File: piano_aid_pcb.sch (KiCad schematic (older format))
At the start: 25 parts, among them J1 Barrel_Jack_MountingPin, J2 Screw_Terminal_01x03, J3 DIN-5_180degree, J4 Conn_01x06_Female, J5 Micro_SD_Card, U1 317030213, U2 6N138, U3 74AHCT1G125SE-7, U4 AZ1117-3.3

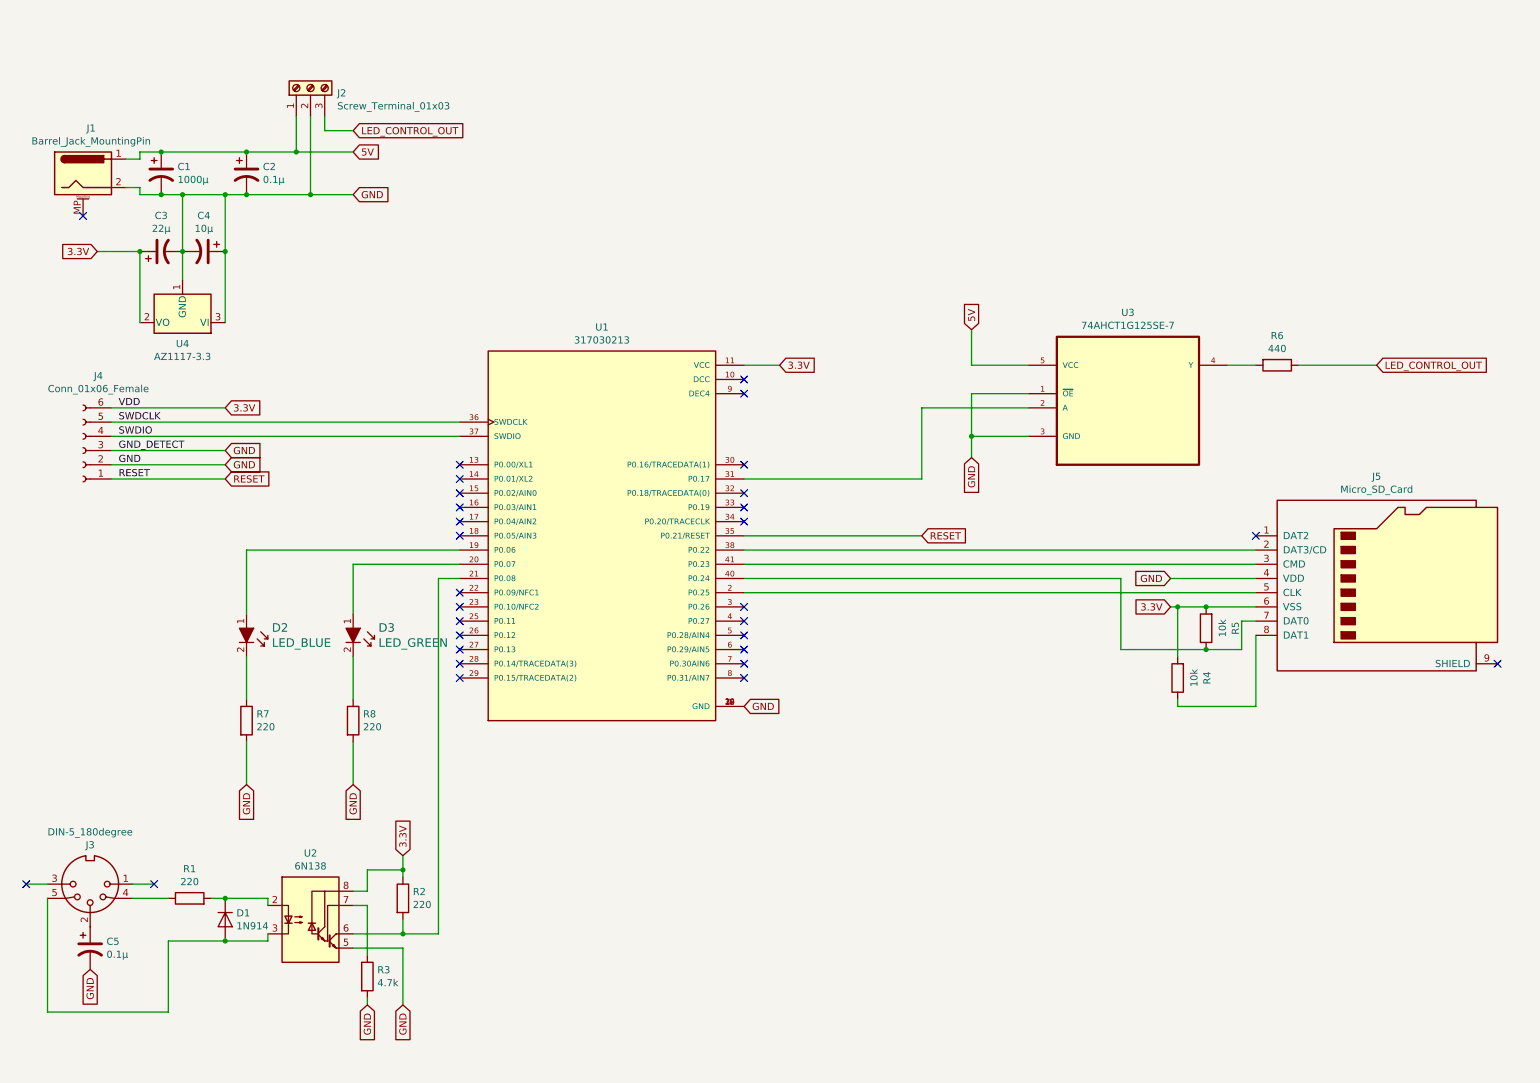
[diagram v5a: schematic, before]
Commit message: Started board layout. Finished footprints
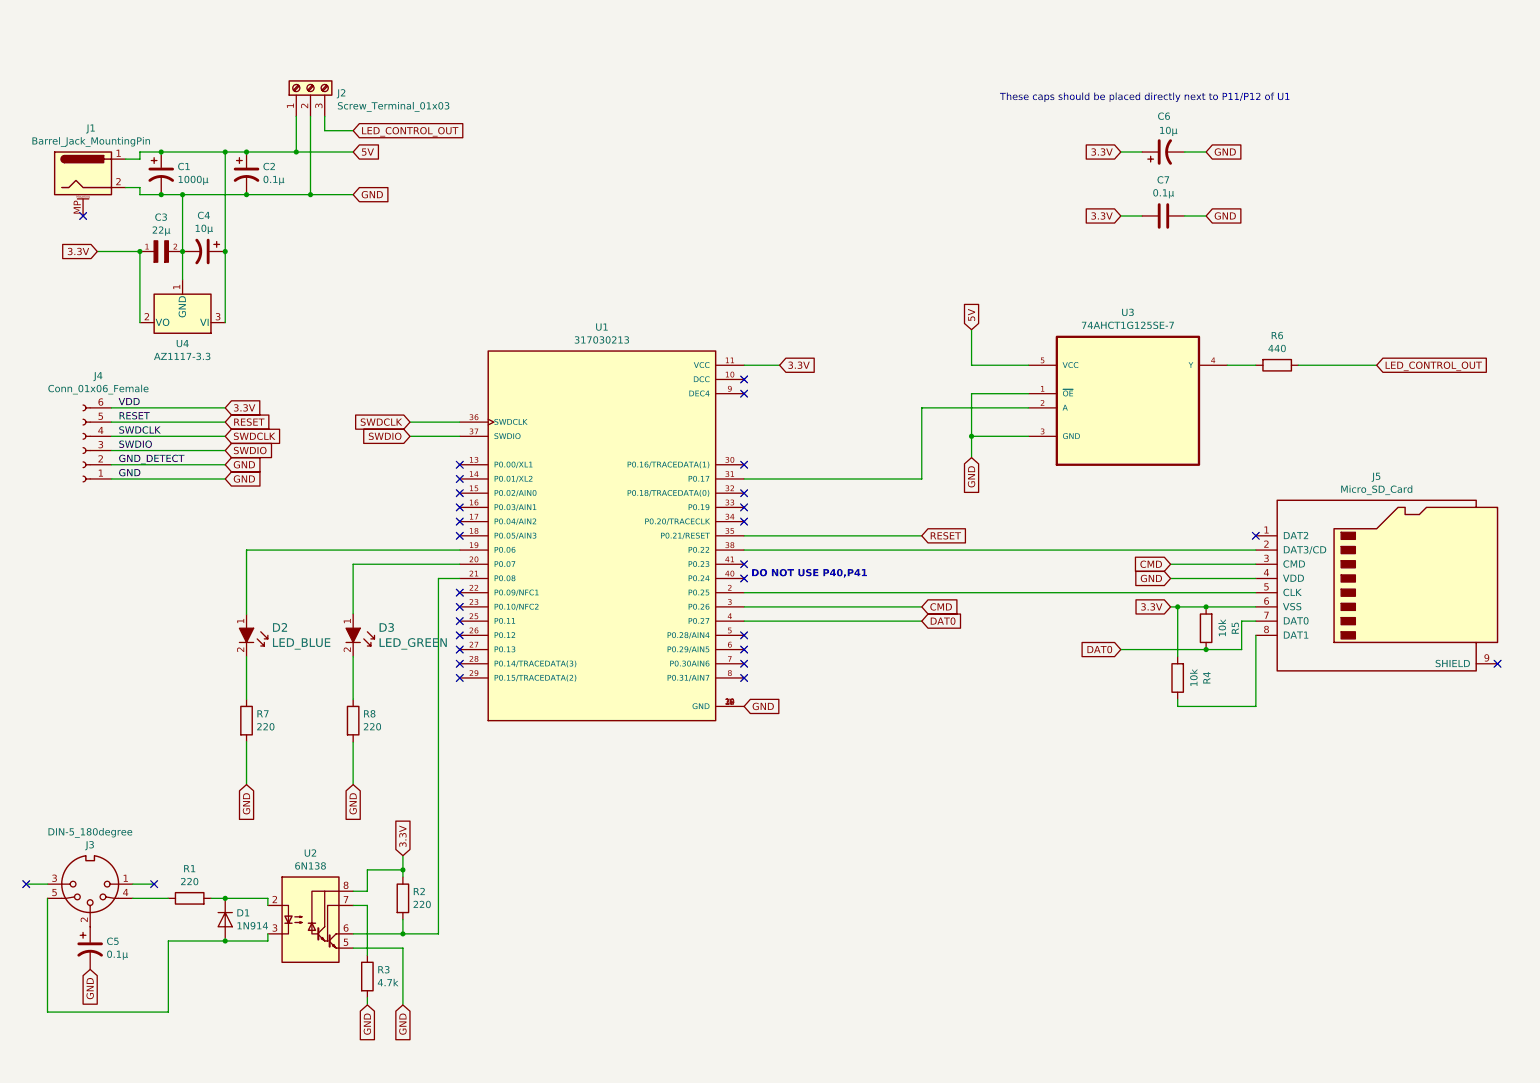
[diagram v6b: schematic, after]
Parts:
- removed C3: 22µ, symbol Device:CP1
- added C3: 22µ, C1206C226M9PACTU:CAPC3216X110N, symbol C1206C226M9PACTU:C1206C226M9PACTU
- added C6: 10µ, Capacitor_SMD:C_0805_2012Metric_Pad1.15x1.40mm_HandSolder, symbol Device:CP1
- added C7: 0.1µ, Capacitor_SMD:C_0805_2012Metric_Pad1.15x1.40mm_HandSolder, symbol Device:C
- C1: footprint (none) -> Capacitor_THT:CP_Radial_D10.0mm_P5.00mm
- C2, C4, C5: footprint (none) -> Capacitor_SMD:C_0805_2012Metric_Pad1.15x1.40mm_HandSolder
- D2, D3: footprint digikey-footprints:0603 -> LED_SMD:LED_0805_2012Metric_Pad1.15x1.40mm_HandSolder
- J4: footprint (none) -> Connector_PinSocket_2.54mm:PinSocket_1x06_P2.54mm_Vertical
- U2: footprint (none) -> Package_DIP:DIP-8_W7.62mm
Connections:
- net 3.3V: now also C3.1, C6.1, C7.2
- net 5V: now also C4.1, U4.3 (VI)
- net GND: now also J4.1 (Pin_1), C3.2, C6.2, C7.1; no longer C4.1, J4.3 (Pin_3), U4.3 (VI)
- net RESET: now also J4.5 (Pin_5); no longer J4.1 (Pin_1)
- net SWDCLK: now also J4.4 (Pin_4); no longer J4.5 (Pin_5)
- net SWDIO: now also J4.3 (Pin_3); no longer J4.4 (Pin_4)
- net CMD: now reaches U1.3 (P0.26)
- net CMD: now also J5.3 (CMD)
- net DAT0: now reaches U1.4 (P0.27)
- net DAT0: now also J5.7 (DAT0), R5.1
- net at U1.41 (P0.23): no longer J5.3 (CMD)
- now unconnected: U1.40 (P0.24)
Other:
- note added: "DO NOT USE P40,P41"
- note added: "These caps should be placed directly next to P11/P12 of U1"
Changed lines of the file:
@@
 F 0 "C1" H 1665 1196 50  0000 L CNN
 F 1 "1000µ" H 1665 1105 50  0000 L CNN
-F 2 "" H 1550 1150 50  0001 C CNN
+F 2 "Capacitor_THT:CP_Radial_D10.0mm_P5.00mm" H 1550 1150 50  0001 C CNN
 F 3 "~" H 1550 1150 50  0001 C CNN
 	1    1550 1150
@@
 	1400 1300 1550 1300
 Wire Wire Line
-	1200 2900 3650 2900
-Wire Wire Line
-	3650 3000 1200 3000
-Wire Wire Line
 	5650 3700 6900 3700
 $Comp
@@
 F 0 "J4" H 892 2575 50  0000 C CNN
 F 1 "Conn_01x06_Female" H 892 2666 50  0000 C CNN
-F 2 "" H 1000 3100 50  0001 C CNN
+F 2 "Connector_PinSocket_2.54mm:PinSocket_1x06_P2.54mm_Vertical" H 1000 3100 50  0001 C CNN
 F 3 "~" H 1000 3100 50  0001 C CNN
 	1    1000 3100
@@
 Text Label 1250 2800 0    50   ~ 0
 VDD
+Text Label 1250 3000 0    50   ~ 0
+SWDCLK
+Text Label 1250 3100 0    50   ~ 0
+SWDIO
+Wire Wire Line
+	1200 3300 2000 3300
+Text Label 1250 3300 0    50   ~ 0
+GND
+Text Label 1250 3200 0    50   ~ 0
+GND_DETECT
 Text Label 1250 2900 0    50   ~ 0
-SWDCLK
-Text Label 1250 3000 0    50   ~ 0
-SWDIO
-Wire Wire Line
-	1200 3200 2000 3200
-Text Label 1250 3200 0    50   ~ 0
-GND
-Text Label 1250 3100 0    50   ~ 0
-GND_DETECT
-Text Label 1250 3300 0    50   ~ 0
 RESET
 $Comp
@@
 $EndComp
 Wire Wire Line
-	1200 3100 2000 3100
+	1200 3200 2000 3200
 Text GLabel 2900 1000 2    50   Input ~ 0
 5V
@@
 Text GLabel 5650 4900 2    50   Input ~ 0
 GND
-Text GLabel 2000 3100 2    50   Input ~ 0
-GND
 Text GLabel 2000 3200 2    50   Input ~ 0
+GND
+Text GLabel 2000 3300 2    50   Input ~ 0
 GND
 Text GLabel 8650 4000 0    50   Input ~ 0
@@
 NoConn ~ 9250 3700
 Wire Wire Line
-	9250 3900 5650 3900
-Wire Wire Line
 	9250 4100 5650 4100
 Wire Wire Line
@@
 	9150 4300 9150 4500
 Connection ~ 8900 4500
-Wire Wire Line
-	8300 4000 8300 4500
-Wire Wire Line
-	5650 4000 8300 4000
 Wire Wire Line
 	8300 4500 8900 4500
@@
 	1550 1300 1700 1300
 Connection ~ 1700 1300
-Wire Wire Line
-	1700 1300 2000 1300
-Connection ~ 2000 1300
 $Comp
 L Device:CP1 C4
@@
 F 0 "C4" V 1598 1700 50  0000 C CNN
 F 1 "10µ" V 1689 1700 50  0000 C CNN
-F 2 "" H 1850 1700 50  0001 C CNN
+F 2 "Capacitor_SMD:C_0805_2012Metric_Pad1.15x1.40mm_HandSolder" H 1850 1700 50  0001 C CNN
 F 3 "~" H 1850 1700 50  0001 C CNN
 	1    1850 1700
 	0    1    1    0
 $EndComp
-$Comp
-L Device:CP1 C3
-U 1 1 6145E06D
-P 1550 1700
-F 0 "C3" V 1802 1700 50  0000 C CNN
-F 1 "22µ" V 1711 1700 50  0000 C CNN
-F 2 "" H 1550 1700 50  0001 C CNN
-F 3 "~" H 1550 1700 50  0001 C CNN
-	1    1550 1700
-	0    -1   -1   0
-$EndComp
 Connection ~ 2000 1700
 Wire Wire Line
@@
 Wire Wire Line
 	1400 1700 1400 2200
-Wire Wire Line
-	2000 1300 2000 1700
 Wire Wire Line
 	1700 1300 1700 1700
@@
 3.3V
 Wire Wire Line
-	1550 1000 2150 1000
+	1550 1000 2000 1000
 Wire Wire Line
 	2500 1000 2900 1000
@@
 Wire Wire Line
 	2600 1300 2900 1300
-Wire Wire Line
-	2000 1300 2150 1300
 Connection ~ 2600 1300
 Wire Wire Line
@@
 Text GLabel 6900 3700 2    50   Input ~ 0
 RESET
-Text GLabel 2000 3300 2    50   Input ~ 0
+Text GLabel 2000 2900 2    50   Input ~ 0
 RESET
 Wire Wire Line
-	1200 3300 2000 3300
+	1200 2900 2000 2900
 $Comp
 L Device:CP1 C2
@@
 F 0 "C2" H 2265 1196 50  0000 L CNN
 F 1 "0.1µ" H 2265 1105 50  0000 L CNN
-F 2 "" H 2150 1150 50  0001 C CNN
+F 2 "Capacitor_SMD:C_0805_2012Metric_Pad1.15x1.40mm_HandSolder" H 2150 1150 50  0001 C CNN
 F 3 "~" H 2150 1150 50  0001 C CNN
 	1    2150 1150
@@
 F 0 "C5" H 1165 6646 50  0000 L CNN
 F 1 "0.1µ" H 1165 6555 50  0000 L CNN
-F 2 "" H 1050 6600 50  0001 C CNN
+F 2 "Capacitor_SMD:C_0805_2012Metric_Pad1.15x1.40mm_HandSolder" H 1050 6600 50  0001 C CNN
 F 3 "~" H 1050 6600 50  0001 C CNN
 	1    1050 6600
@@
 F 0 "U2" H 2600 6867 50  0000 C CNN
 F 1 "6N138" H 2600 6776 50  0000 C CNN
-F 2 "" H 2890 6100 50  0001 C CNN
+F 2 "Package_DIP:DIP-8_W7.62mm" H 2890 6100 50  0001 C CNN
 F 3 "http://www.onsemi.com/pub/Collateral/HCPL2731-D.pdf" H 2890 6100 50  0001 C CNN
 	1    2600 6400
@@
 NoConn ~ 5650 3500
 NoConn ~ 5650 3600
-NoConn ~ 5650 4200
-NoConn ~ 5650 4300
 NoConn ~ 5650 4400
 NoConn ~ 5650 4500
@@
 F 0 "D2" V 2047 4628 60  0000 L CNN
 F 1 "LED_BLUE" V 2153 4628 60  0000 L CNN
-F 2 "digikey-footprints:0603" H 2350 4650 60  0001 L CNN
+F 2 "LED_SMD:LED_0805_2012Metric_Pad1.15x1.40mm_HandSolder" H 2350 4650 60  0001 L CNN
 F 3 "http://optoelectronics.liteon.com/upload/download/DS22-2000-230/LTST-C191TBKT.pdf" H 2350 4750 60  0001 L CNN
 F 4 "160-1647-1-ND" H 2350 4850 60  0001 L CNN "Digi-Key_PN"
@@
 F 0 "D3" V 2797 4628 60  0000 L CNN
 F 1 "LED_GREEN" V 2903 4628 60  0000 L CNN
-F 2 "digikey-footprints:0603" H 3100 4650 60  0001 L CNN
+F 2 "LED_SMD:LED_0805_2012Metric_Pad1.15x1.40mm_HandSolder" H 3100 4650 60  0001 L CNN
 F 3 "https://dammedia.osram.info/media/resource/hires/osram-dam-2493945/LG%20L29K.pdf" H 3100 4750 60  0001 L CNN
 F 4 "475-2709-1-ND" H 3100 4850 60  0001 L CNN "Digi-Key_PN"
@@
 	0    1    1    0
 $EndComp
+Text GLabel 8300 1000 0    50   Input ~ 0
+3.3V
+Text GLabel 8900 1000 2    50   Input ~ 0
+GND
+$Comp
+L Device:CP1 C6
+U 1 1 614E35CA
+P 8600 1000
+F 0 "C6" V 8850 950 50  0000 L CNN
+F 1 "10µ" V 8750 900 50  0000 L CNN
+F 2 "Capacitor_SMD:C_0805_2012Metric_Pad1.15x1.40mm_HandSolder" H 8600 1000 50  0001 C CNN
+F 3 "~" H 8600 1000 50  0001 C CNN
+	1    8600 1000
+	0    -1   -1   0
+$EndComp
+Wire Wire Line
+	8750 1000 8900 1000
+Wire Wire Line
+	8300 1000 8450 1000
+$Comp
+L Device:C C7
+U 1 1 614E98EF
+P 8600 1450
+F 0 "C7" V 8348 1450 50  0000 C CNN
+F 1 "0.1µ" V 8439 1450 50  0000 C CNN
+F 2 "Capacitor_SMD:C_0805_2012Metric_Pad1.15x1.40mm_HandSolder" H 8638 1300 50  0001 C CNN
+F 3 "~" H 8600 1450 50  0001 C CNN
+	1    8600 1450
+	0    1    1    0
+$EndComp
+Text GLabel 8300 1450 0    50   Input ~ 0
+3.3V
+Text GLabel 8900 1450 2    50   Input ~ 0
+GND
+Wire Wire Line
+	8450 1450 8300 1450
+Wire Wire Line
+	8750 1450 8900 1450
+$Comp
+L C1206C226M9PACTU:C1206C226M9PACTU C3
+U 1 1 614F3A2A
+P 1500 1700
+F 0 "C3" H 1550 1940 50  0000 C CNN
+F 1 "22µ" H 1550 1849 50  0000 C CNN
+F 2 "C1206C226M9PACTU:CAPC3216X110N" H 1500 1700 50  0001 L BNN
+F 3 "" H 1500 1700 50  0001 L BNN
+	1    1500 1700
+	1    0    0    -1
+$EndComp
+Text GLabel 8650 3900 0    50   Input ~ 0
+CMD
+Wire Wire Line
+	8650 3900 9250 3900
+Wire Wire Line
+	5650 4200 6900 4200
+Text GLabel 6900 4200 2    50   Input ~ 0
+CMD
+Text GLabel 8300 4500 0    50   Input ~ 0
+DAT0
+Wire Wire Line
+	5650 4300 6900 4300
+Text GLabel 6900 4300 2    50   Input ~ 0
+DAT0
+NoConn ~ 5650 3900
+NoConn ~ 5650 4000
+Text Notes 7450 650  0    50   ~ 0
+These caps should be placed directly next to P11/P12 of U1
+Text Notes 5700 4000 0    50   ~ 10
+DO NOT USE P40,P41
+Text GLabel 3300 2900 0    50   Input ~ 0
+SWDCLK
+Text GLabel 3300 3000 0    50   Input ~ 0
+SWDIO
+Text GLabel 2000 3100 2    50   Input ~ 0
+SWDIO
+Text GLabel 2000 3000 2    50   Input ~ 0
+SWDCLK
+Wire Wire Line
+	1200 3100 2000 3100
+Wire Wire Line
+	1200 3000 2000 3000
+Wire Wire Line
+	3300 2900 3650 2900
+Wire Wire Line
+	3300 3000 3650 3000
+Connection ~ 2000 1000
+Wire Wire Line
+	2000 1000 2150 1000
+Wire Wire Line
+	2000 1000 2000 1700
+Wire Wire Line
+	1700 1300 2150 1300
 $EndSCHEMATC

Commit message: Made PCB. Not happy with the traces, may try again. For now this is 95% complete.
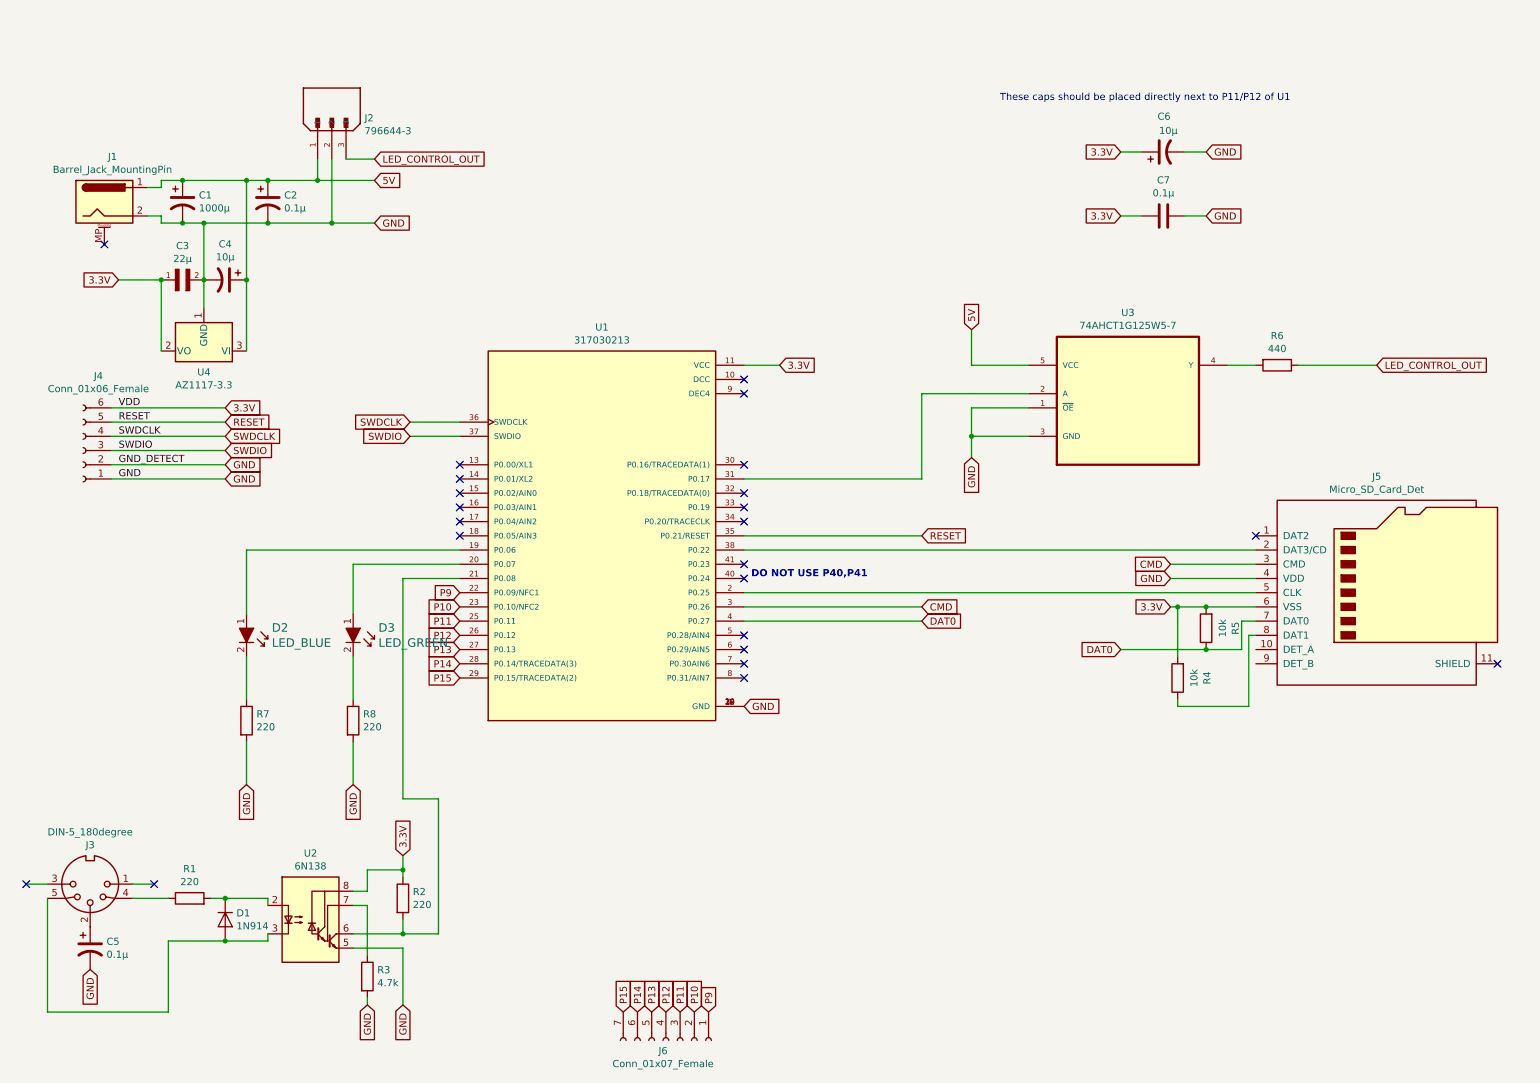
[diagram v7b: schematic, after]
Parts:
- removed J2: Screw_Terminal_01x03, TerminalBlock:TerminalBlock_bornier-3_P5.08mm, symbol Connector:Screw_Terminal_01x03
- removed J5: Micro_SD_Card, adafruit:MICROSD, symbol Connector:Micro_SD_Card
- removed U1: 317030213, micro:XCVR_317030213, symbol piano_aid_pcb-rescue:317030213-317030213
- removed U3: 74AHCT1G125SE-7, 74AHCT1G125SE-7:SOT65P210X110-5N, symbol 74AHCT1G125SE-7:74AHCT1G125SE-7
- added J2: 796644-3, 796644-3:TE_796644-3, symbol 796644-3:796644-3
- added J5: Micro_SD_Card_Det, adafruit:MICROSD, symbol Connector:Micro_SD_Card_Det
- added J6: Conn_01x07_Female, Connector_PinSocket_2.54mm:PinSocket_1x07_P2.54mm_Vertical, symbol Connector:Conn_01x07_Female
- added U1: 317030213, micro:XCVR_317030213, symbol 317030213:317030213
- added U3: 74AHCT1G125W5-7, 74AHCT1G125W5-7:SOT95P280X140-5N, symbol 74AHCT1G125W5-7:74AHCT1G125W5-7
- U4: footprint 2021-09-23_22-23-04:AZ1117IH-3.3TRG1 -> eec:Diodes_Inc.-SOT223-03_2017-0-MFG
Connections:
- net 3.3V: now also J5.6 (VSS), U1.11 (VCC)
- net 5V: now also J2.1, U3.5 (VCC)
- net CMD: now also J5.3 (CMD), U1.3 (P0.26)
- net DAT0: now also J5.7 (DAT0), U1.4 (P0.27)
- net GND: now also J2.2, J5.4 (VDD), U1.1 (GND), U1.12 (GND), U1.24 (GND), U1.39 (GND), U3.1 (~OE), U3.3 (GND)
- net LED_CONTROL_OUT: now also J2.3
- net RESET: now also U1.35 (P0.21/RESET)
- net SWDCLK: now also U1.36 (SWDCLK)
- net SWDIO: now also U1.37 (SWDIO)
- net at D2.1: now also U1.19 (P0.06)
- net at D3.1: now also U1.20 (P0.07)
- net at R2.2, U2.6 (VO2): now also U1.21 (P0.08)
- net at R4.1: now also J5.8 (DAT1)
- net at R6.2: now also U3.4 (Y)
- new net: J5.5 (CLK), U1.2 (P0.25)
- new net: U1.31 (P0.17), U3.2 (A)
- new net: J5.2 (DAT3/CD), U1.38 (P0.22)
- new net P10: J6.2 (Pin_2), U1.23 (P0.10/NFC2)
- new net P11: J6.3 (Pin_3), U1.25 (P0.11)
- new net P12: J6.4 (Pin_4), U1.26 (P0.12)
- new net P13: J6.5 (Pin_5), U1.27 (P0.13)
- new net P14: J6.6 (Pin_6), U1.28 (P0.14/TRACEDATA(3))
- new net P15: J6.7 (Pin_7), U1.29 (P0.15/TRACEDATA(2))
- new net P9: J6.1 (Pin_1), U1.22 (P0.09/NFC1)
- no-connect marks 30 -> 23
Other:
- moved on the sheet: C1, C2, C3, C4, U4
